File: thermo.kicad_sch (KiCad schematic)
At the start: 23 parts, among them U1 ESP32-C6, U2 W25Q128JVS, Y1 40M, Y2 32k768

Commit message: add UART series resistor
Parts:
- added R4: 470, symbol Device:R
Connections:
- net at U1.29 (U0TXD/GPIO16/FSPICS0): now also R4.1
- net U0RXD: now reaches U1.30 (U0RXD/GPIO17/FSPICS1)
- new net U0TXD: R4.2
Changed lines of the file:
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@@
+	(wire
+		(pts
+			(xy 161.29 72.39) (xy 140.97 72.39)
+		)
+		(stroke
+			(width 0)
+			(type default)
+		)
+	)
 	(wire
 		(pts
@@
 	(wire
 		(pts
+			(xy 140.97 69.85) (xy 144.78 69.85)
+		)
+		(stroke
+			(width 0)
+			(type default)
+		)
+	)
+	(wire
+		(pts
 			(xy 21.59 110.49) (xy 21.59 111.76)
 		)
@@
 		(pts
 			(xy 31.75 92.71) (xy 29.21 92.71)
+		)
+		(stroke
+			(width 0)
+			(type default)
+		)
+	)
+	(wire
+		(pts
+			(xy 152.4 69.85) (xy 161.29 69.85)
 		)
 		(stroke
@@
 		)
 	)
+	(label "U0TXD"
+		(at 161.29 69.85 180)
+		(effects
+			(font
+				(size 1.27 1.27)
+			)
+			(justify right bottom)
+		)
+	)
 	(label "XTAL_32K_N"
 		(at 53.34 55.88 180)
+		(effects
+			(font
+				(size 1.27 1.27)
+			)
+			(justify right bottom)
+		)
+	)
+	(label "U0RXD"
+		(at 161.29 72.39 180)
 		(effects
 			(font
@@
 					(unit 1)
 				)
+			)
+		)
+	)
+	(symbol
+		(lib_id "Device:R")
+		(at 148.59 69.85 90)
+		(unit 1)
+		(exclude_from_sim no)
+		(in_bom yes)
+		(on_board yes)
+		(dnp no)
+		(fields_autoplaced yes)
+		(property "Reference" "R4"
+			(at 148.59 63.5 90)
+			(effects
+				(font
+					(size 1.27 1.27)
+				)
+			)
+		)
+		(property "Value" "470"
+			(at 148.59 66.04 90)
+			(effects
+				(font
+					(size 1.27 1.27)
+				)
+			)
+		)
+		(property "Footprint" ""
+			(at 148.59 71.628 90)
+			(effects
+				(font
+					(size 1.27 1.27)
+				)
+				(hide yes)
+			)
+		)
+		(property "Datasheet" "~"
+			(at 148.59 69.85 0)
+			(effects
+				(font
+					(size 1.27 1.27)
+				)
+				(hide yes)
+			)
+		)
+		(property "Description" "Resistor"
+			(at 148.59 69.85 0)
+			(effects
+				(font
+					(size 1.27 1.27)
+				)
+				(hide yes)
+			)
+		)
+		(pin "2"
+		)
+		(pin "1"
+		)
+		(instances
+			(project ""
+				(path "/fde4d48d-460a-4d76-9ab6-1824c1ad585e"
+					(reference "R4")
+					(unit 1)
+				)

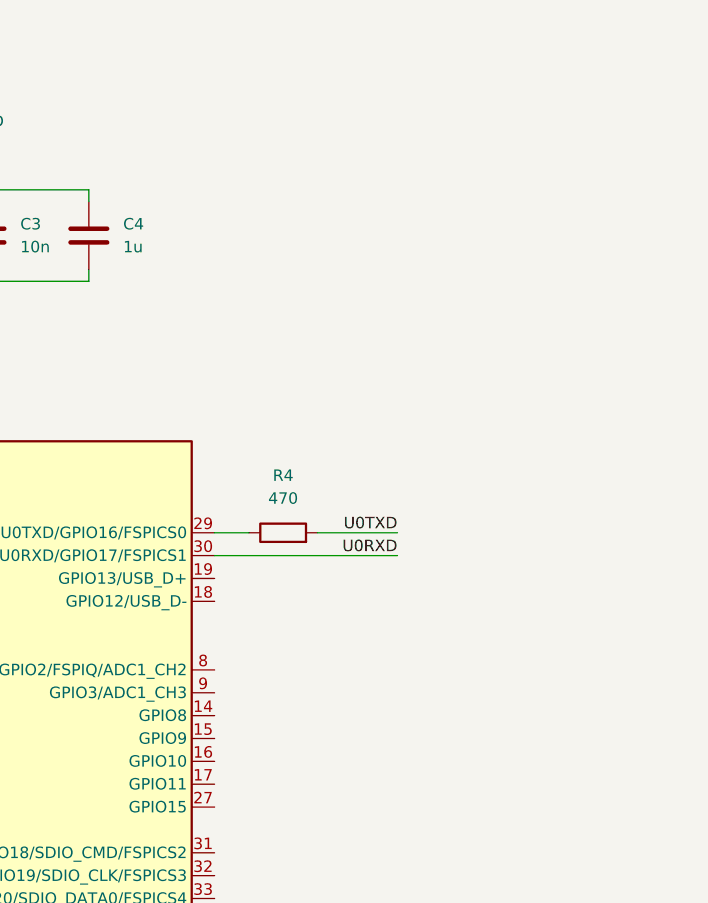
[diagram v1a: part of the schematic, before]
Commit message: add uart auto download
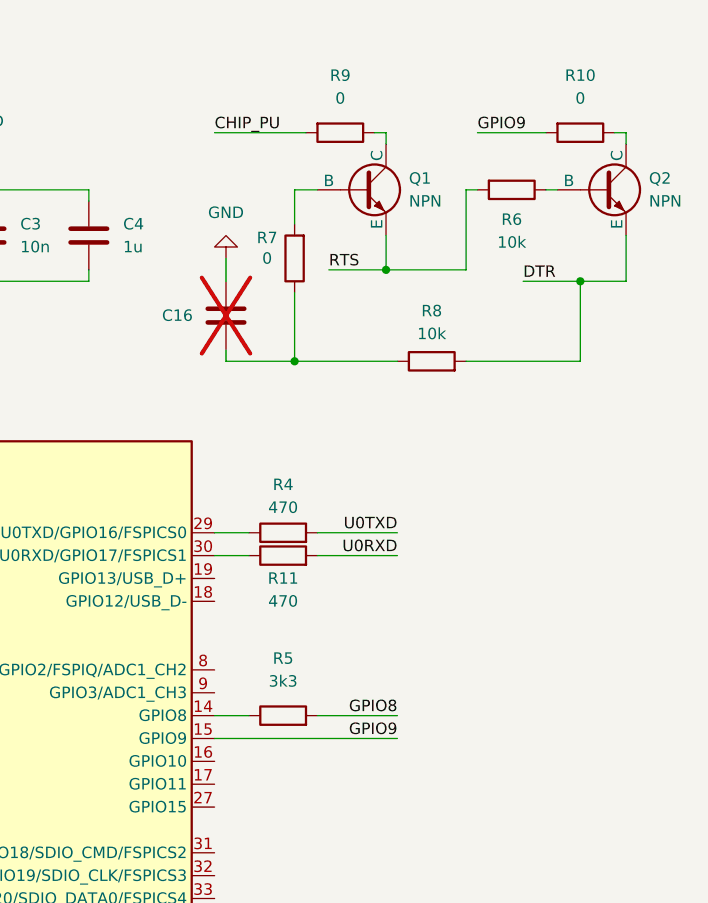
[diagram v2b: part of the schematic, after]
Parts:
- added C16: ~, symbol Device:C
- added Q1, Q2: NPN, symbol Simulation_SPICE:NPN
- added R10, R7, R9: 0, symbol Device:R
- added R11: 470, symbol Device:R
- added R5: 3k3, symbol Device:R
- added R6, R8: 10k, symbol Device:R
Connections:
- net GND: now also C16.2
- net U0RXD: now also R11.2; no longer U1.30 (U0RXD/GPIO17/FSPICS1)
- net at U1.14 (GPIO8): now also R5.1
- net GPIO9: now reaches U1.15 (GPIO9)
- net GPIO9: now also R10.2
- new net: Q2.1 (C), R10.1
- new net: Q2.2 (B), R6.1
- new net: Q1.1 (C), R9.1
- new net: Q1.2 (B), R7.2
- new net: R11.1, U1.30 (U0RXD/GPIO17/FSPICS1)
- new net: C16.1, R7.1, R8.1
- new net CHIP_PU: R9.2
- new net DTR: Q2.3 (E), R8.2
- new net GPIO8: R5.2
- new net RTS: Q1.3 (E), R6.2

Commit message: add integrated usb connector
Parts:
- added J1: USB_C_Receptacle_USB2.0_14P, symbol Connector:USB_C_Receptacle_USB2.0_14P
- added R12, R13: 5k1, symbol Device:R
- added U3: USBLC6-2SC6, Package_TO_SOT_SMD:SOT-23-6, symbol Power_Protection:USBLC6-2SC6
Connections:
- net GND: now also J1.A1 (GND), J1.A12 (GND), J1.B1 (GND), J1.B12 (GND), R12.1, R13.1, U3.2 (GND)
- net USB_D-: now reaches U1.18 (GPIO12/USB_D-)
- net USB_D-: now also U3.6 (I/O1)
- net USB_D+: now reaches U1.19 (GPIO13/USB_D+)
- net USB_D+: now also U3.4 (I/O2)
- new net: J1.A5 (CC1), R12.2
- new net: J1.B5 (CC2), R13.2
- new net: J1.A4 (VBUS), J1.A9 (VBUS), J1.B4 (VBUS), J1.B9 (VBUS), U3.5 (VBUS)
- new net: J1.A6 (D+), J1.B6 (D+), U3.3 (I/O2)
- new net: J1.A7 (D-), J1.B7 (D-), U3.1 (I/O1)

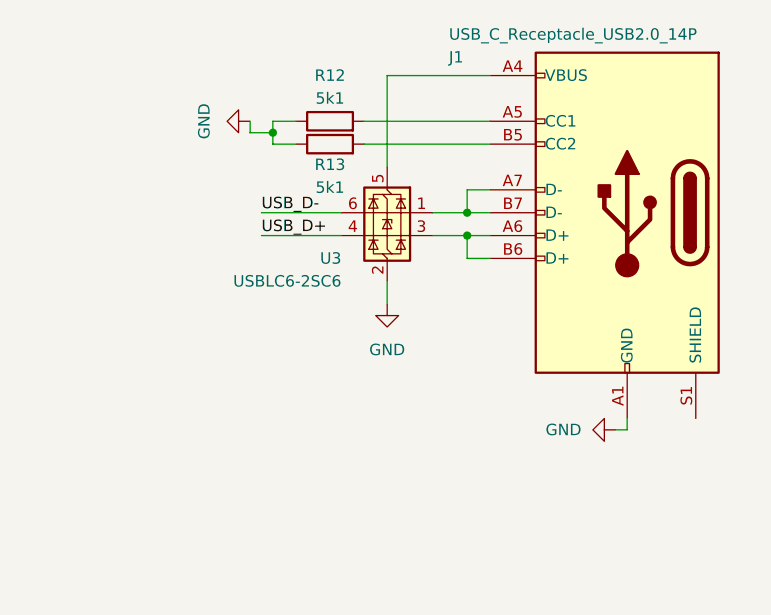
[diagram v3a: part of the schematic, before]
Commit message: add vbus and 5v net to usb connector
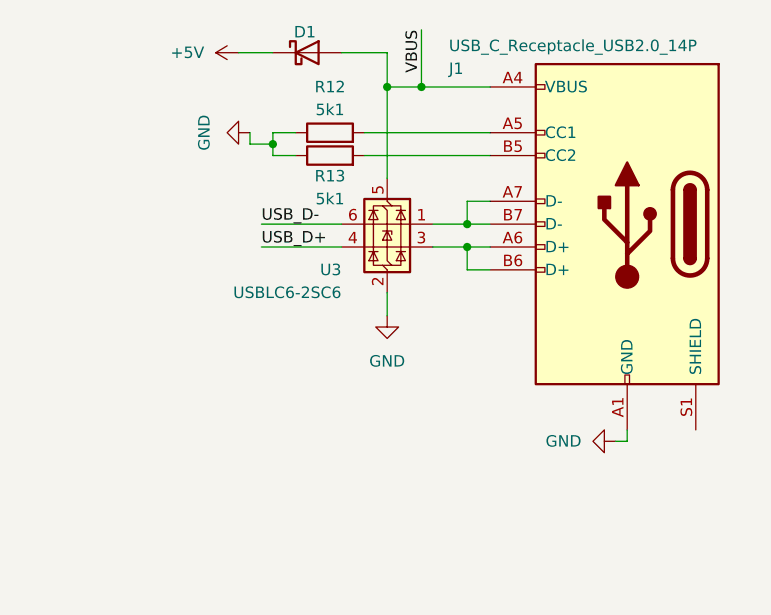
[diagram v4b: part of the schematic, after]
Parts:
- added D1: D_Schottky, symbol Device:D_Schottky
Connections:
- net VBUS: now reaches J1.A4 (VBUS), J1.A9 (VBUS), J1.B4 (VBUS), J1.B9 (VBUS), U3.5 (VBUS)
- net VBUS: now also D1.2 (A)
- new net +5V: D1.1 (K)
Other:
- moved on the sheet: J1, R12, R13, U3
